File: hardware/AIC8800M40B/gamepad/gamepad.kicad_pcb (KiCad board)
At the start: 2 copper layers, 155.8 x 76.2 mm, 88 parts, among them J1 Rumble_TL, J10 Conn_01x14, J11 Micro_SD_Card_Det1, J12 Conn_01x05, J13 Conn_01x06, J2 Rumble_ML, J3 Rumble_TR, J4 Rumble_MR, J7 Conn_01x03, J8 Conn_01x03, J9 Conn_02x15_Odd_Even, Q1 AO3402, Q2 AO3402, Q3 AO3402, Q4 AO3402, SW1 SW_Push, SW10 SW_Push, SW11 SW_Push, SW12 SW_Push, SW13 SW_Push, SW14 SW_Push, SW15 SW_Push, SW2 SW_Push, SW3 SW_Push, SW4 SW_Push, SW6 SW_Push, SW7 SW_Push, SW8 SW_Push, SW9 SW_Push, U1 74HC595, U2 74HC165, U3 74HC165, U4 ADS7830

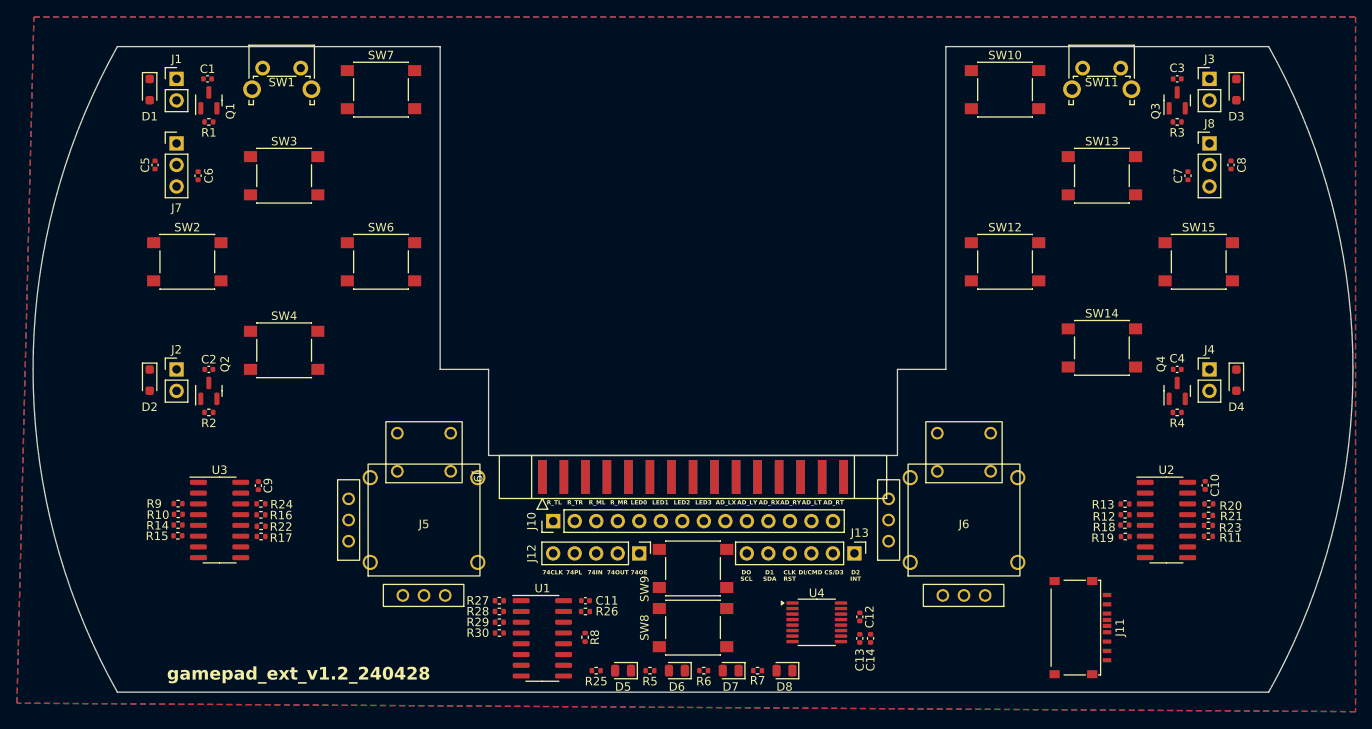
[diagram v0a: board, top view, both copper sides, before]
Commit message: [hardware/gamepad] update pcb
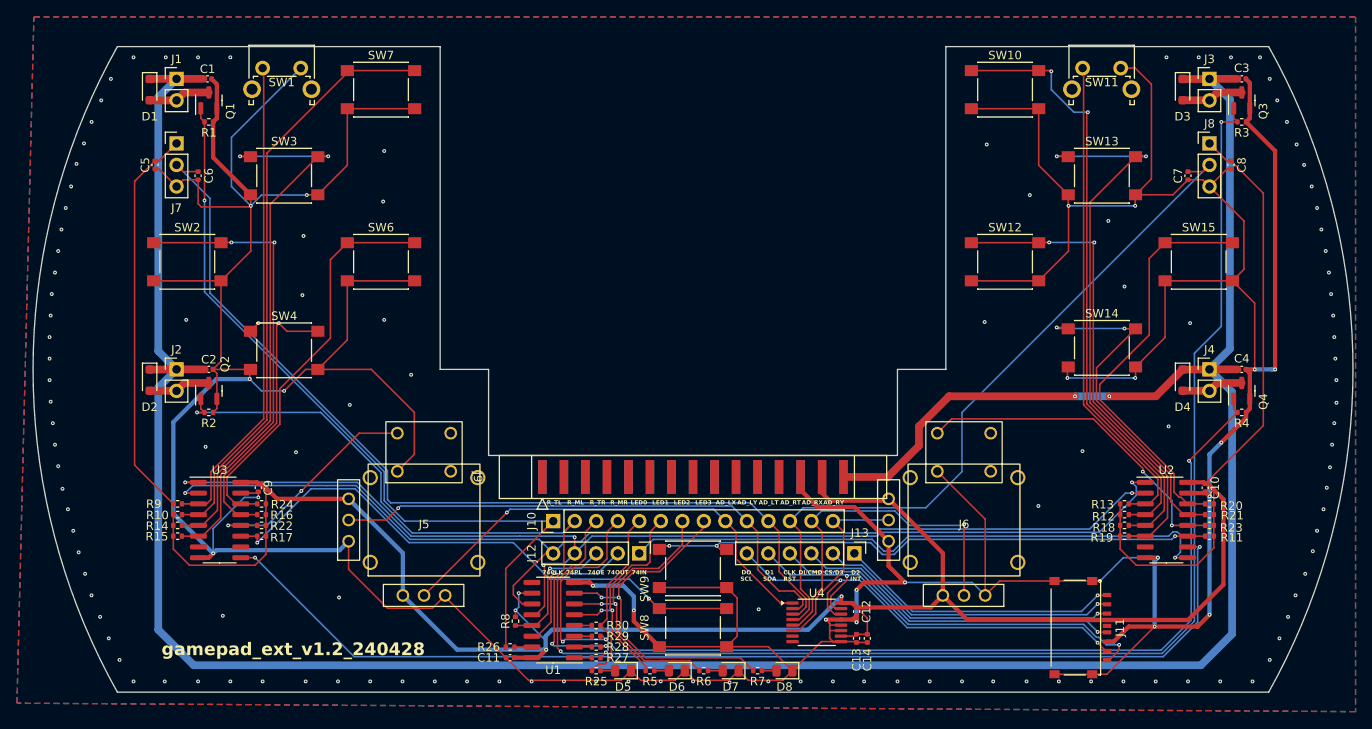
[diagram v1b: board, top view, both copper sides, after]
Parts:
- moved R27 13.3 mm to (166.4, 135.6), turned to 0 degrees
- moved R28 12.2 mm to (166.4, 134.4), turned to 0 degrees
- moved R29 11.5 mm to (166.4, 133.1), turned to 0 degrees
- moved R30 11.5 mm to (166.4, 131.8), turned to 0 degrees
- moved C11 11.1 mm to (156.2, 135.6), turned to 180 degrees
- moved R26 9.83 mm to (156.2, 134.4), turned to 180 degrees
- moved R8 8.43 mm to (156.8, 131.3), turned to 90 degrees
- moved C3 7.62 mm to (242.6, 67.3), turned to 0 degrees
- moved C4 7.62 mm to (242.6, 101.6), turned to 0 degrees
- moved Q3 7.62 mm to (242.6, 69.8)
- moved Q4 7.62 mm to (242.6, 104.1)
- moved R3 7.62 mm to (242.6, 72.4)
- moved R4 7.62 mm to (242.6, 106.7)
- moved D3 6.35 mm to (235.6, 68.6)
- moved D4 6.35 mm to (235.6, 102.9)
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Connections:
- net /5V renamed /VBAT
- J10 pad 11: /AD_RX -> /AD_LT
- J10 pad 12: /AD_RY -> /AD_RT
- J10 pad 13: /AD_LT -> /AD_RX
- J10 pad 14: /AD_RT -> /AD_RY
- J10 pad 2: /RUMBLE_TR -> /RUMBLE_ML
- J10 pad 3: /RUMBLE_ML -> /RUMBLE_TR
- J12 pad 1: /74OE -> /74IN
- J12 pad 3: /74IN -> /74OE
- U4 pad 3: /AD_RX -> /AD_LT
- U4 pad 4: /AD_RY -> /AD_RT
- U4 pad 5: /AD_LT -> /AD_RX
- U4 pad 6: /AD_RT -> /AD_RY
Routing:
- net GND: track 0.00 -> 692.1 mm, vias 0 -> 145
- net /VCC: track 0.00 -> 341.4 mm, vias 0 -> 4
- net /VBAT: track 0.00 -> 338.8 mm, vias 0 -> 2
- net /RUMBLE_TR: track 0.00 -> 159.3 mm, vias 0 -> 3
- net /74PL: track 0.00 -> 135.6 mm, vias 0 -> 4
- net /74CLK: track 0.00 -> 131.5 mm, vias 0 -> 2
- net Net-(U2-DS): track 0.00 -> 129.9 mm, vias 0 -> 2
- net /RUMBLE_MR: track 0.00 -> 124.6 mm, vias 0 -> 3
- net /AD_LT: track 0.00 -> 112.6 mm
- net /RUMBLE_TL: track 0.00 -> 93.4 mm, vias 0 -> 1
- net /AD_RT: track 0.00 -> 87.7 mm
- net /RUMBLE_ML: track 0.00 -> 78.5 mm, vias 0 -> 3
- net /SW_MR: track 0.00 -> 71.2 mm, vias 0 -> 2
- net /74IN: track 0.00 -> 70.7 mm, vias 0 -> 1
- net /SW_ML: track 0.00 -> 69.9 mm
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
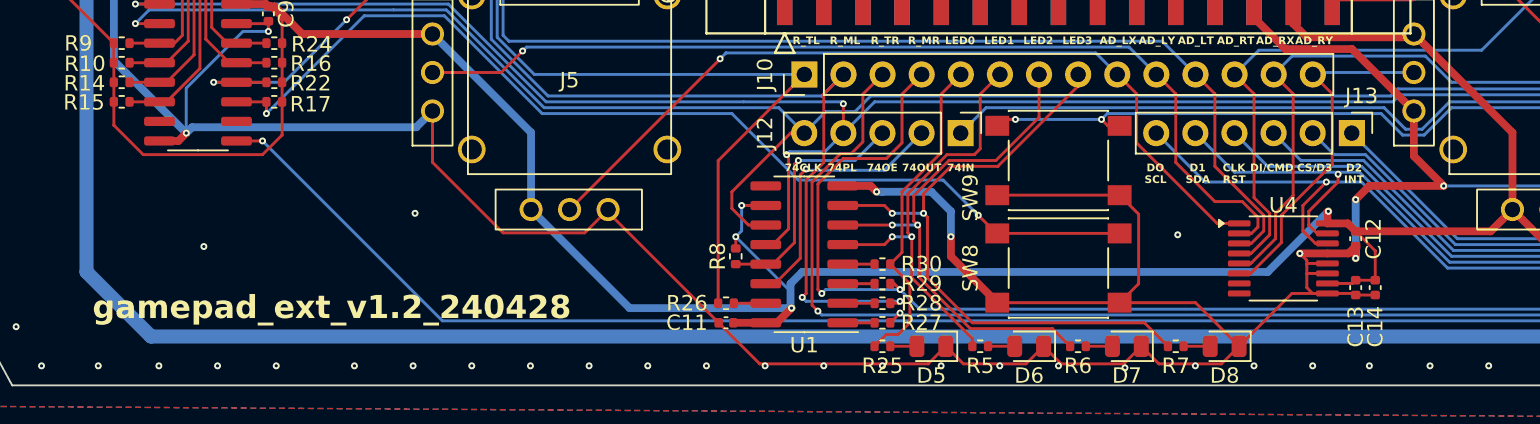
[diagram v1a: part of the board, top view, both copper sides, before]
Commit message: [hardware/gamepad] add pull-up resister to I2C
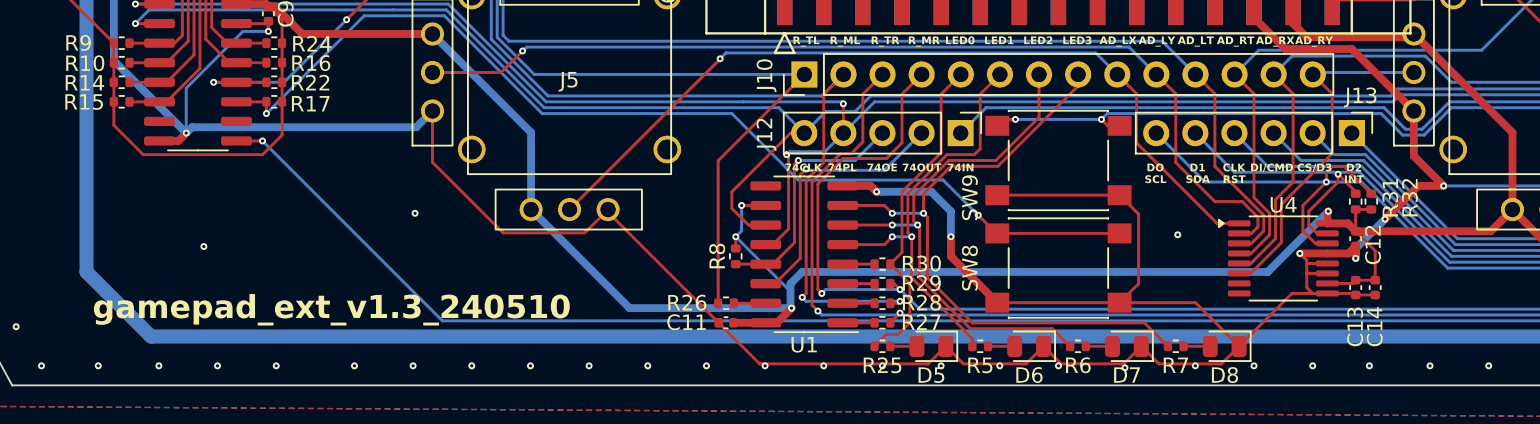
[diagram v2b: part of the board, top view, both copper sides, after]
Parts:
- added R31: 4.7K, Resistor_SMD:R_0402_1005Metric, F.Cu at (197.1, 127.8)
- added R32: 4.7K, Resistor_SMD:R_0402_1005Metric, F.Cu at (198.1, 127.8)
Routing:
- net /DO: track 53.1 -> 57.6 mm
- net /VCC: track 341.4 -> 343.9 mm
- net GND: track 692.1 -> 690.3 mm
- net /SDA: track 54.7 -> 56.5 mm
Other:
- board text added: "gamepad_ext_v1.3_240510"
- board text removed: "gamepad_ext_v1.2_240428"

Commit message: [hardware/gamepad] minor tweak
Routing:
- net /VBAT: vias 2 -> 4
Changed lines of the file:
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@@
+	)
+	(segment
+		(start 226.949 104.775)
+		(end 227.584 104.775)
+		(width 0.9144)
+		(layer "F.Cu")
+		(net 92)
 	)
 	(segment
@@
 	)
 	(segment
-		(start 222.885 104.775)
-		(end 208.026 104.775)
+		(start 208.026 104.775)
+		(end 222.25 104.775)
 		(width 0.9144)
 		(layer "F.Cu")
@@
 	)
 	(segment
+		(start 222.25 104.775)
+		(end 222.885 104.775)
+		(width 0.9144)
+		(layer "F.Cu")
+		(net 92)
+	)
+	(segment
+		(start 116.84 101.6)
+		(end 120.17 101.6)
+		(width 0.9144)
+		(layer "F.Cu")
+		(net 92)
+	)
+	(segment
 		(start 232.43 104.775)
 		(end 235.585 101.62)
@@
 	)
 	(segment
-		(start 116.84 101.6)
-		(end 120.17 101.6)
-		(width 0.9144)
-		(layer "F.Cu")
-		(net 92)
-	)
-	(segment
 		(start 204.47 108.331)
 		(end 204.47 110.617)
@@
 	)
 	(segment
+		(start 227.584 104.775)
+		(end 232.43 104.775)
+		(width 0.9144)
+		(layer "F.Cu")
+		(net 92)
+	)
+	(segment
 		(start 200.787 114.3)
 		(end 195.58 114.3)
@@
 	)
 	(segment
-		(start 226.949 104.775)
-		(end 232.43 104.775)
-		(width 0.9144)
-		(layer "F.Cu")
-		(net 92)
-	)
-	(segment
 		(start 113.665 101.62)
 		(end 116.82 101.62)
@@
 	)
 	(via
+		(at 222.25 104.775)
+		(size 0.45085)
+		(drill 0.2032)
+		(layers "F.Cu" "B.Cu")
+		(net 92)
+	)
+	(via
+		(at 227.584 104.775)
+		(size 0.45085)
+		(drill 0.2032)
+		(layers "F.Cu" "B.Cu")
+		(net 92)
+	)
+	(via
 		(at 222.885 104.775)
 		(size 0.45085)
@@
 	)
 	(segment
+		(start 222.885 104.775)
+		(end 226.949 104.775)
+		(width 0.9144)
+		(layer "B.Cu")
+		(net 92)
+	)
+	(segment
 		(start 114.681 99.441)
 		(end 116.84 101.6)
@@
 		(width 0.9144)
 		(layer "B.Cu")
-		(net 92)
-	)
-	(segment
-		(start 222.885 104.775)
-		(end 226.949 104.775)
-		(width 0.9144)
-		(layer "B.Cu")

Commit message: {hardware/gamepad] update
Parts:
- added C15: 0.1uF, Capacitor_SMD:C_0402_1005Metric, F.Cu at (135.1, 120.7)
- added C16: 0.1uF, Capacitor_SMD:C_0402_1005Metric, F.Cu at (147.3, 130.3)
- added C17: 0.1uF, Capacitor_SMD:C_0402_1005Metric, F.Cu at (198.9, 119.1)
- added C18: 0.1uF, Capacitor_SMD:C_0402_1005Metric, F.Cu at (211.1, 130.3)
- added R33: 2K, Resistor_SMD:R_0402_1005Metric, F.Cu at (134.6, 116.8)
- added R34: 2K, Resistor_SMD:R_0402_1005Metric, F.Cu at (144.0, 130.3)
- added R35: 2K, Resistor_SMD:R_0402_1005Metric, F.Cu at (198.9, 116.8)
- added R36: 2K, Resistor_SMD:R_0402_1005Metric, F.Cu at (207.8, 130.3)
- added R37: 2K, Resistor_SMD:R_0402_1005Metric, F.Cu at (114.3, 75.4)
- added R38: 2K, Resistor_SMD:R_0402_1005Metric, F.Cu at (241.3, 75.4)
- C6: value 10pF -> 0.1nF
- C7: value 10pF -> 0.1uF
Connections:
- J5 pad 3: /VCC -> Net-(J5-Pad3)
- J5 pad 6: /VCC -> Net-(J5-Pad6)
- J6 pad 3: /VCC -> Net-(J6-Pad3)
- J6 pad 6: /VCC -> Net-(J6-Pad6)
- J7 pad 1: /VCC -> Net-(J7-Pin_1)
- J8 pad 1: /VCC -> Net-(J8-Pin_1)
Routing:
- net GND: track 690.3 -> 696.9 mm
- net Net-(J8-Pin_1): track 0.00 -> 2.80 mm
- net Net-(J7-Pin_1): track 0.00 -> 2.54 mm
- net Net-(J6-Pad3): track 0.00 -> 2.43 mm
- net /AD_RX: track 42.4 -> 44.7 mm
- net /AD_LY: track 63.5 -> 65.8 mm
- net /AD_LX: track 54.2 -> 56.5 mm
- net /AD_RY: track 23.0 -> 25.3 mm
- net Net-(J6-Pad6): track 0.00 -> 2.23 mm
- net Net-(J5-Pad3): track 0.00 -> 2.04 mm
- net Net-(J5-Pad6): track 0.00 -> 2.04 mm
- net /VCC: track 343.9 -> 342.5 mm, vias 4 -> 6
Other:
- board text added: "gamepad_ext_v1.4_241014"
- board text removed: "gamepad_ext_v1.3_240510"
